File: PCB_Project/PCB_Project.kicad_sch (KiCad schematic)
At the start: 1 part

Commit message: ignore how ugly it looks I need to fix it
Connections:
- net +3V3: now reaches U4.1 (3V3)
- net +3V3: now also U4.17 (3V3)
- net Pi_RX: now reaches U4.10 (GPIO_15_RXD)
- net I2C_SCL_1: now reaches U4.11 (GPIO_17)
- net I2C_SDA_1: now reaches U4.13 (GPIO_27)
- net GND: now reaches U4.14 (GND)
- net GND: now also U4.20 (GND), U4.25 (GND), U4.30 (GND), U4.34 (GND), U4.39 (GND), U4.6 (GND), U4.9 (GND)
- net +5V: now reaches U4.2 (5V)
- net +5V: now also U4.4 (5V)
- net I2C_SCL_2: now reaches U4.27 (GPIO_0_ID_SD)
- net I2C_SDA_2: now reaches U4.29 (GPIO_5)
- net I2C_SDA_M: now reaches U4.3 (GPIO_2_(SDA))
- net I2C_SCL_M: now reaches U4.5 (GPIO_3_(SCL))
- net Pi_TX: now reaches U4.8 (GPIO_14_TXD)
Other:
- moved on the sheet: U4

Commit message: work baby
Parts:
- added R1, R2, R4, R5, R8, R9: 5k, Resistor_SMD:R_0603_1608Metric, symbol Device:R
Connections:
- net +3V3: now also R1.1, R2.1, R4.1, R5.1, R8.1, R9.1
- net I2C_SCL_1: now also U4.3 (GPIO_2_(SDA)), R4.2; no longer U4.11 (GPIO_17)
- net I2C_SCL_2: now also U4.29 (GPIO_5), R1.2; no longer U4.27 (GPIO_0_ID_SD)
- net I2C_SCL_M: now also U4.28 (GPIO_1_(ID_SC)), R9.2; no longer U4.5 (GPIO_3_(SCL))
- net I2C_SDA_1: now also U4.5 (GPIO_3_(SCL)), R5.2; no longer U4.13 (GPIO_27)
- net I2C_SDA_2: now also U4.7 (GPIO_4_(GPCLK0)), R2.2; no longer U4.29 (GPIO_5)
- net I2C_SDA_M: now also U4.27 (GPIO_0_ID_SD), R8.2; no longer U4.3 (GPIO_2_(SDA))
- net CSB_Gryo_BMI088: now reaches U4.24 (GPIO_8_(CE0))
- net CSB_Accel_BMI088: now reaches U4.26 (GPIO_7_(CE1))
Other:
- removed sheet motor_driver

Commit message: 2 footprints left then can design
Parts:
- R1, R2, R4, R5, R8, R9: footprint Resistor_SMD:R_0603_1608Metric -> Resistor_SMD:R_0402_1005Metric
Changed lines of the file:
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@@
 			)
 		)
-		(property "Footprint" "Resistor_SMD:R_0603_1608Metric"
+		(property "Footprint" "Resistor_SMD:R_0402_1005Metric"
 			(at 101.092 71.12 90)
 			(effects
@@
 			)
 		)
-		(property "Footprint" "Resistor_SMD:R_0603_1608Metric"
+		(property "Footprint" "Resistor_SMD:R_0402_1005Metric"
 			(at 182.372 67.31 90)
 			(effects
@@
 			)
 		)
-		(property "Footprint" "Resistor_SMD:R_0603_1608Metric"
+		(property "Footprint" "Resistor_SMD:R_0402_1005Metric"
 			(at 103.378 43.18 90)
 			(effects
@@
 			)
 		)
-		(property "Footprint" "Resistor_SMD:R_0603_1608Metric"
+		(property "Footprint" "Resistor_SMD:R_0402_1005Metric"
 			(at 83.058 39.37 90)
 			(effects
@@
 			)
 		)
-		(property "Footprint" "Resistor_SMD:R_0603_1608Metric"
+		(property "Footprint" "Resistor_SMD:R_0402_1005Metric"
 			(at 79.502 25.4 90)
 			(effects
@@
 			)
 		)
-		(property "Footprint" "Resistor_SMD:R_0603_1608Metric"
+		(property "Footprint" "Resistor_SMD:R_0402_1005Metric"
 			(at 104.648 85.09 90)
 			(effects

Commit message: pcb work
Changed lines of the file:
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@@
+		)
+	)
+	(text_box "I missed pin 12"
+		(exclude_from_sim no)
+		(at 177.8 36.83 0)
+		(size 12.065 8.255)
+		(stroke
+			(width 0)
+			(type default)
+		)
+		(fill
+			(type none)
+		)
+		(effects
+			(font
+				(size 1.27 1.27)
+			)
+			(justify left top)
 		)
 	)

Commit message: more cleaning up and adding footprints
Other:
- moved on the sheet: R9

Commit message: need to fix the one damn footprint
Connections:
- net CSB_Gryo_BMI088: now also U4.11 (GPIO_17); no longer U4.24 (GPIO_8_(CE0))
- net SCK_1: now also U4.23 (GPIO_11)
- net SCLK_2: now also U4.40 (GPIO_21)
- net SDI_1: now also U4.19 (GPIO_10)
- net SDI_2: now also U4.38 (GPIO_20)
- net SDO_1: now also U4.21 (GPIO_9)
- net SDO_2: now also U4.35 (GPIO_19)
- net nCS_2: now also U4.12 (GPIO_18)
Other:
- removed sheet Power_Management
- moved on the sheet: R1, R2, R4, R5, R8, R9

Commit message: re commit
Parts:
- U4: footprint Connector_PinHeader_2.54mm:PinHeader_2x20_P2.54mm_Vertical -> Connector_PinSocket_2.54mm:PinSocket_2x20_P2.54mm_Vertical
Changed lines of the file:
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@@
-	)
-	(junction
-		(at 115.57 76.2)
-		(diameter 0)
-		(color 0 0 0 0)
 	)
 	(junction
@@
 	(wire
 		(pts
+			(xy 86.36 38.1) (xy 115.57 38.1)
+		)
+		(stroke
+			(width 0)
+			(type default)
+		)
+	)
+	(wire
+		(pts
+			(xy 161.29 41.91) (xy 158.75 41.91)
+		)
+		(stroke
+			(width 0)
+			(type default)
+		)
+	)
+	(wire
+		(pts
+			(xy 161.29 72.39) (xy 158.75 72.39)
+		)
+		(stroke
+			(width 0)
+			(type default)
+		)
+	)
+	(wire
+		(pts
+			(xy 185.42 76.2) (xy 189.23 76.2)
+		)
+		(stroke
+			(width 0)
+			(type default)
+		)
+	)
+	(wire
+		(pts
+			(xy 111.76 64.77) (xy 115.57 64.77)
+		)
+		(stroke
+			(width 0)
+			(type default)
+		)
+	)
+	(wire
+		(pts
+			(xy 115.57 72.39) (xy 113.03 72.39)
+		)
+		(stroke
+			(width 0)
+			(type default)
+		)
+	)
+	(wire
+		(pts
+			(xy 158.75 26.67) (xy 161.29 26.67)
+		)
+		(stroke
+			(width 0)
+			(type default)
+		)
+	)
+	(wire
+		(pts
+			(xy 158.75 60.96) (xy 161.29 60.96)
+		)
+		(stroke
+			(width 0)
+			(type default)
+		)
+	)
+	(wire
+		(pts
+			(xy 66.04 29.21) (xy 66.04 30.48)
+		)
+		(stroke
+			(width 0)
+			(type default)
+		)
+	)
+	(wire
+		(pts
+			(xy 66.04 30.48) (xy 115.57 30.48)
+		)
+		(stroke
+			(width 0)
+			(type default)
+		)
+	)
+	(wire
+		(pts
+			(xy 158.75 80.01) (xy 161.29 80.01)
+		)
+		(stroke
+			(width 0)
+			(type default)
+		)
+	)
+	(wire
+		(pts
+			(xy 66.04 35.56) (xy 66.04 34.29)
+		)
+		(stroke
+			(width 0)
+			(type default)
+		)
+	)
+	(wire
+		(pts
+			(xy 91.44 80.01) (xy 93.98 80.01)
+		)
+		(stroke
+			(width 0)
+			(type default)
+		)
+	)
+	(wire
+		(pts
+			(xy 161.29 99.06) (xy 158.75 99.06)
+		)
+		(stroke
+			(width 0)
+			(type default)
+		)
+	)
+	(wire
+		(pts
+			(xy 111.76 60.96) (xy 115.57 60.96)
+		)
+		(stroke
+			(width 0)
+			(type default)
+		)
+	)
+	(wire
+		(pts
+			(xy 83.82 38.1) (xy 86.36 38.1)
+		)
+		(stroke
+			(width 0)
+			(type default)
+		)
+	)
+	(wire
+		(pts
+			(xy 93.98 74.93) (xy 93.98 76.2)
+		)
+		(stroke
+			(width 0)
+			(type default)
+		)
+	)
+	(wire
+		(pts
+			(xy 158.75 38.1) (xy 161.29 38.1)
+		)
+		(stroke
+			(width 0)
+			(type default)
+		)
+	)
+	(wire
+		(pts
 			(xy 93.98 76.2) (xy 115.57 76.2)
 		)
@@
 	(wire
 		(pts
-			(xy 86.36 38.1) (xy 115.57 38.1)
-		)
-		(stroke
-			(width 0)
-			(type default)
-		)
-	)
-	(wire
-		(pts
-			(xy 161.29 41.91) (xy 158.75 41.91)
-		)
-		(stroke
-			(width 0)
-			(type default)
-		)
-	)
-	(wire
-		(pts
-			(xy 161.29 72.39) (xy 158.75 72.39)
-		)
-		(stroke
-			(width 0)
-			(type default)
-		)
-	)
-	(wire
-		(pts
-			(xy 185.42 76.2) (xy 189.23 76.2)
-		)
-		(stroke
-			(width 0)
-			(type default)
-		)
-	)
-	(wire
-		(pts
-			(xy 111.76 64.77) (xy 115.57 64.77)
-		)
-		(stroke
-			(width 0)
-			(type default)
-		)
-	)
-	(wire
-		(pts
-			(xy 115.57 72.39) (xy 113.03 72.39)
-		)
-		(stroke
-			(width 0)
-			(type default)
-		)
-	)
-	(wire
-		(pts
-			(xy 158.75 26.67) (xy 161.29 26.67)
-		)
-		(stroke
-			(width 0)
-			(type default)
-		)
-	)
-	(wire
-		(pts
-			(xy 158.75 60.96) (xy 161.29 60.96)
-		)
-		(stroke
-			(width 0)
-			(type default)
-		)
-	)
-	(wire
-		(pts
-			(xy 66.04 29.21) (xy 66.04 30.48)
-		)
-		(stroke
-			(width 0)
-			(type default)
-		)
-	)
-	(wire
-		(pts
-			(xy 66.04 30.48) (xy 115.57 30.48)
-		)
-		(stroke
-			(width 0)
-			(type default)
-		)
-	)
-	(wire
-		(pts
-			(xy 158.75 80.01) (xy 161.29 80.01)
-		)
-		(stroke
-			(width 0)
-			(type default)
-		)
-	)
-	(wire
-		(pts
-			(xy 66.04 35.56) (xy 66.04 34.29)
-		)
-		(stroke
-			(width 0)
-			(type default)
-		)
-	)
-	(wire
-		(pts
-			(xy 91.44 80.01) (xy 93.98 80.01)
-		)
-		(stroke
-			(width 0)
-			(type default)
-		)
-	)
-	(wire
-		(pts
-			(xy 161.29 99.06) (xy 158.75 99.06)
-		)
-		(stroke
-			(width 0)
-			(type default)
-		)
-	)
-	(wire
-		(pts
-			(xy 111.76 60.96) (xy 115.57 60.96)
-		)
-		(stroke
-			(width 0)
-			(type default)
-		)
-	)
-	(wire
-		(pts
-			(xy 83.82 38.1) (xy 86.36 38.1)
-		)
-		(stroke
-			(width 0)
-			(type default)
-		)
-	)
-	(wire
-		(pts
-			(xy 93.98 74.93) (xy 93.98 76.2)
-		)
-		(stroke
-			(width 0)
-			(type default)
-		)
-	)
-	(wire
-		(pts
-			(xy 158.75 38.1) (xy 161.29 38.1)
-		)
-		(stroke
-			(width 0)
-			(type default)
-		)
-	)
-	(wire
-		(pts
 			(xy 86.36 46.99) (xy 86.36 48.26)
 		)
@@
 		(pts
 			(xy 113.03 26.67) (xy 115.57 26.67)
-		)
-		(stroke
-			(width 0)
-			(type default)
-		)
-	)
-	(wire
-		(pts
-			(xy 121.92 76.2) (xy 115.57 76.2)
 		)
 		(stroke
@@
 			)
 		)
-		(property "Footprint" "Connector_PinHeader_2.54mm:PinHeader_2x20_P2.54mm_Vertical"
+		(property "Footprint" "Connector_PinSocket_2.54mm:PinSocket_2x20_P2.54mm_Vertical"
 			(at 120.65 25.4 0)
 			(effects

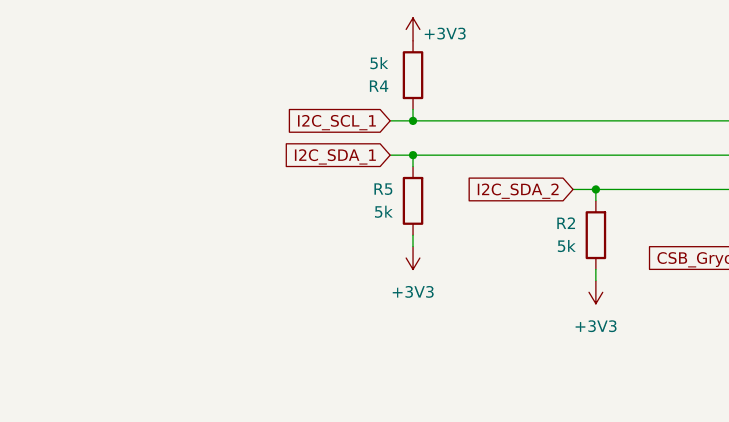
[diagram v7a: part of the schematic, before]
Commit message: Swapped I2C_SDA_1 and I2C_SCL_1
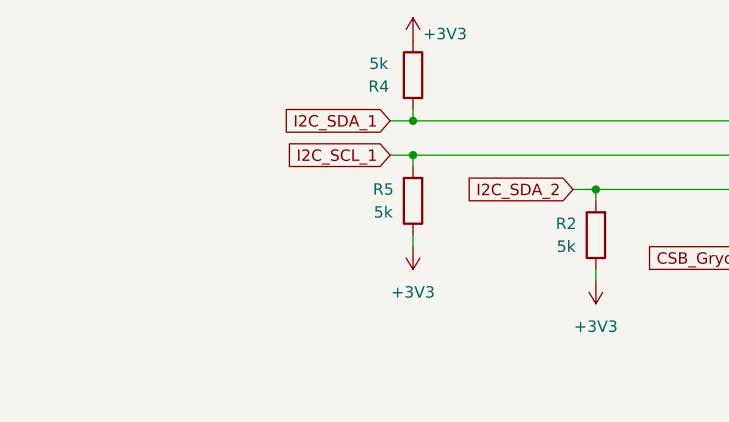
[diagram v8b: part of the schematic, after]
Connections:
- net I2C_SCL_1: now also R5.2, U4.5 (GPIO_3); no longer R4.2, U4.3 (GPIO_2)
- net I2C_SDA_1: now also R4.2, U4.3 (GPIO_2); no longer R5.2, U4.5 (GPIO_3)
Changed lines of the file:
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@@
 	(global_label "I2C_SDA_1"
 		(shape input)
-		(at 63.5 34.29 180)
+		(at 63.5 30.48 180)
 		(fields_autoplaced yes)
 		(effects
@@
 		)
 		(property "Intersheetrefs" "${INTERSHEET_REFS}"
-			(at 50.7177 34.29 0)
+			(at 50.7177 30.48 0)
 			(effects
 				(font
@@
 	(global_label "I2C_SCL_1"
 		(shape input)
-		(at 63.5 30.48 180)
+		(at 63.5 34.29 180)
 		(fields_autoplaced yes)
 		(effects
@@
 		)
 		(property "Intersheetrefs" "${INTERSHEET_REFS}"
-			(at 50.7782 30.48 0)
+			(at 50.7782 34.29 0)
 			(effects
 				(font
